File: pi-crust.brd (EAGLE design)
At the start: 41.9 x 40.4 mm, 10 parts

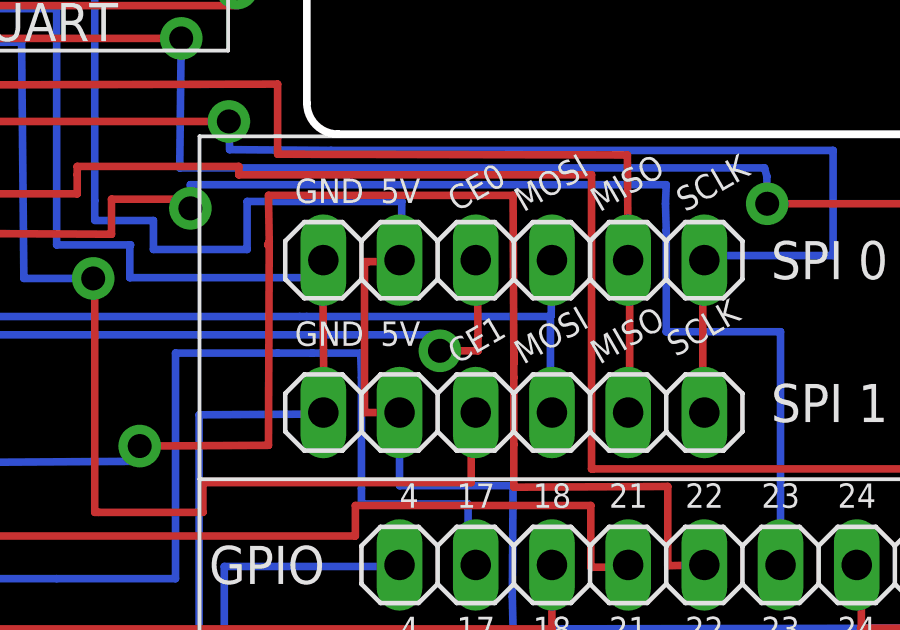
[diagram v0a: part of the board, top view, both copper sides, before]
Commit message: Moved one of the vias so its not so close to the headers.
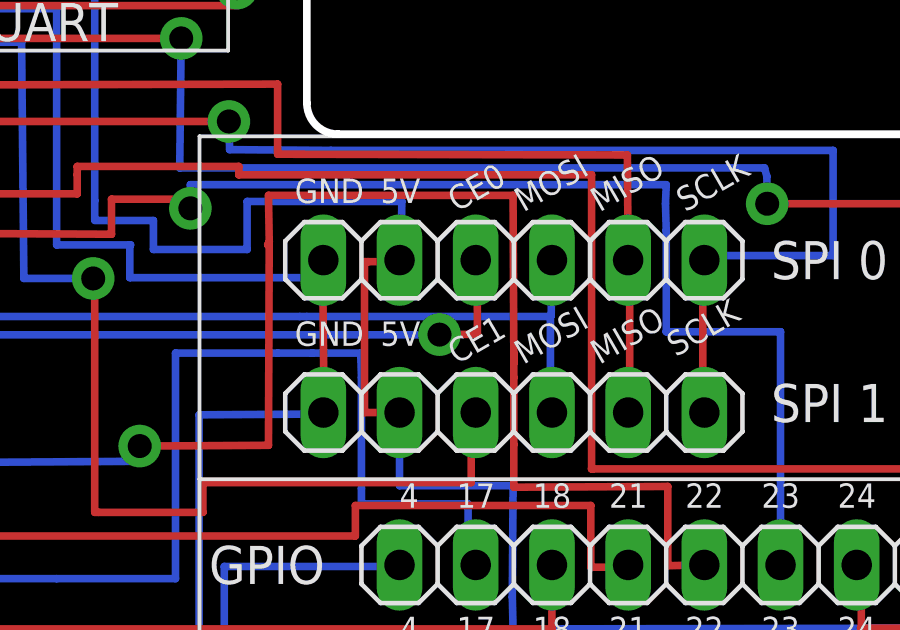
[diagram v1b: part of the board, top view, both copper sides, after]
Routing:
- net SPI_CE_0: track 34.8 -> 33.7 mm
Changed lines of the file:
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@@
 <setting verticaltext="up"/>
 </settings>
-<grid distance="0.02" unitdist="inch" unit="inch" style="lines" multiple="1" display="yes" altdistance="0.025" altunitdist="inch" altunit="inch"/>
+<grid distance="0" unitdist="inch" unit="inch" style="lines" multiple="1" display="yes" altdistance="0.025" altunitdist="inch" altunit="inch"/>
 <layers>
 <layer number="1" name="Top" color="4" fill="1" visible="yes" active="yes"/>
@@
 <wire x1="3.81" y1="23.7744" x2="7.8232" y2="23.7744" width="0.254" layer="16"/>
 <wire x1="24.1808" y1="26.6192" x2="23.9776" y2="26.6192" width="0.254" layer="1"/>
-<wire x1="24.2062" y1="24.13" x2="24.1808" y2="26.6192" width="0.254" layer="1"/>
-<wire x1="22.9362" y1="23.6474" x2="24.2062" y2="23.6474" width="0.254" layer="1"/>
-<wire x1="24.2062" y1="23.6474" x2="24.2062" y2="24.13" width="0.254" layer="1"/>
-<wire x1="22.7584" y1="23.6474" x2="22.9362" y2="23.6474" width="0.254" layer="16"/>
-<wire x1="22.7838" y1="24.1808" x2="22.7584" y2="23.6474" width="0.254" layer="16"/>
+<wire x1="24.18458125" y1="24.1948625" x2="24.1808" y2="26.6192" width="0.254" layer="1"/>
+<wire x1="22.9217875" y1="24.187909375" x2="22.901875" y2="24.195115625" width="0.254" layer="1"/>
+<wire x1="22.901875" y1="24.195115625" x2="24.18458125" y2="24.1948625" width="0.254" layer="1"/>
+<wire x1="22.880903125" y1="24.1807" x2="22.9217875" y2="24.187909375" width="0.254" layer="16"/>
+<wire x1="22.7838" y1="24.1808" x2="22.880903125" y2="24.1807" width="0.254" layer="16"/>
 <wire x1="7.8232" y1="24.1808" x2="22.7838" y2="24.1808" width="0.254" layer="16"/>
 <wire x1="7.8232" y1="23.7744" x2="7.8232" y2="24.1808" width="0.254" layer="16"/>
-<via x="22.9362" y="23.6474" extent="1-16" drill="0.8" diameter="1.4224"/>
+<via x="22.9217875" y="24.187909375" extent="1-16" drill="0.8" diameter="1.4224"/>
 </signal>
 <signal name="3V3">

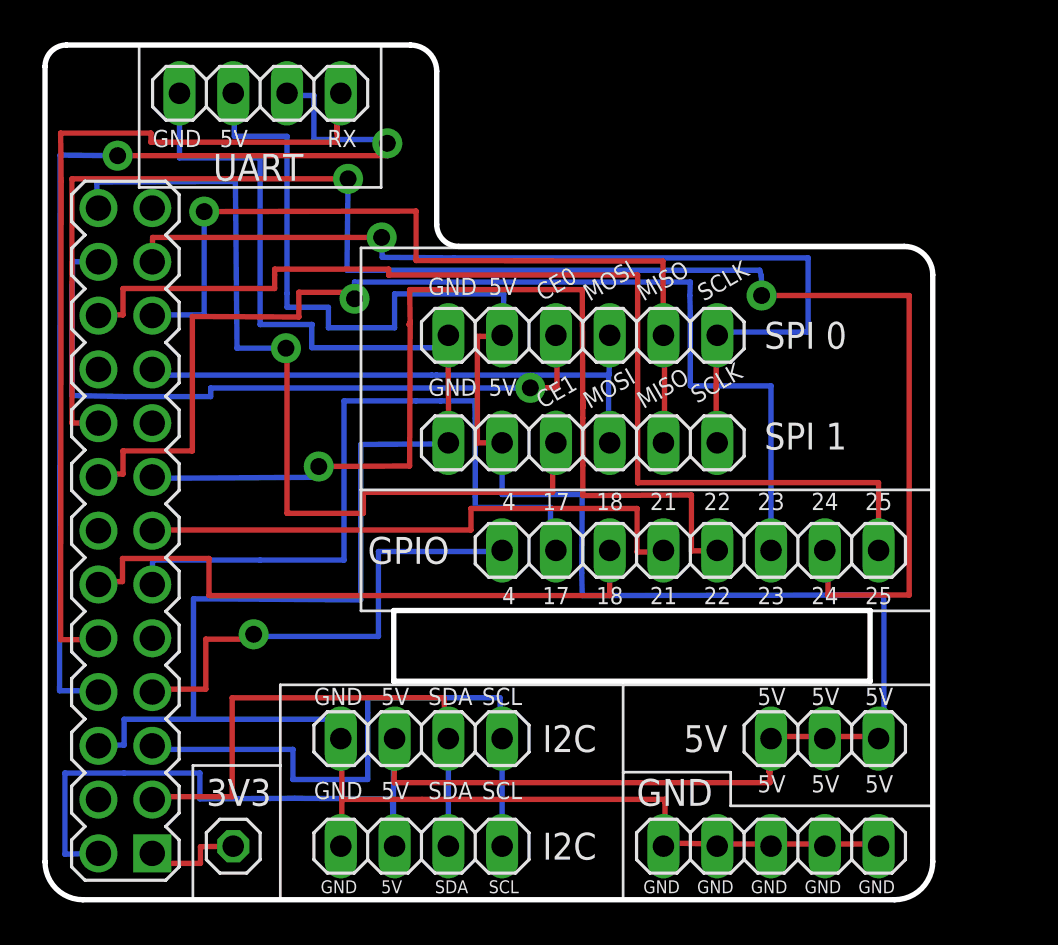
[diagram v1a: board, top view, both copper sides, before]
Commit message: Elongate board slot, as it was a wee bit too short.
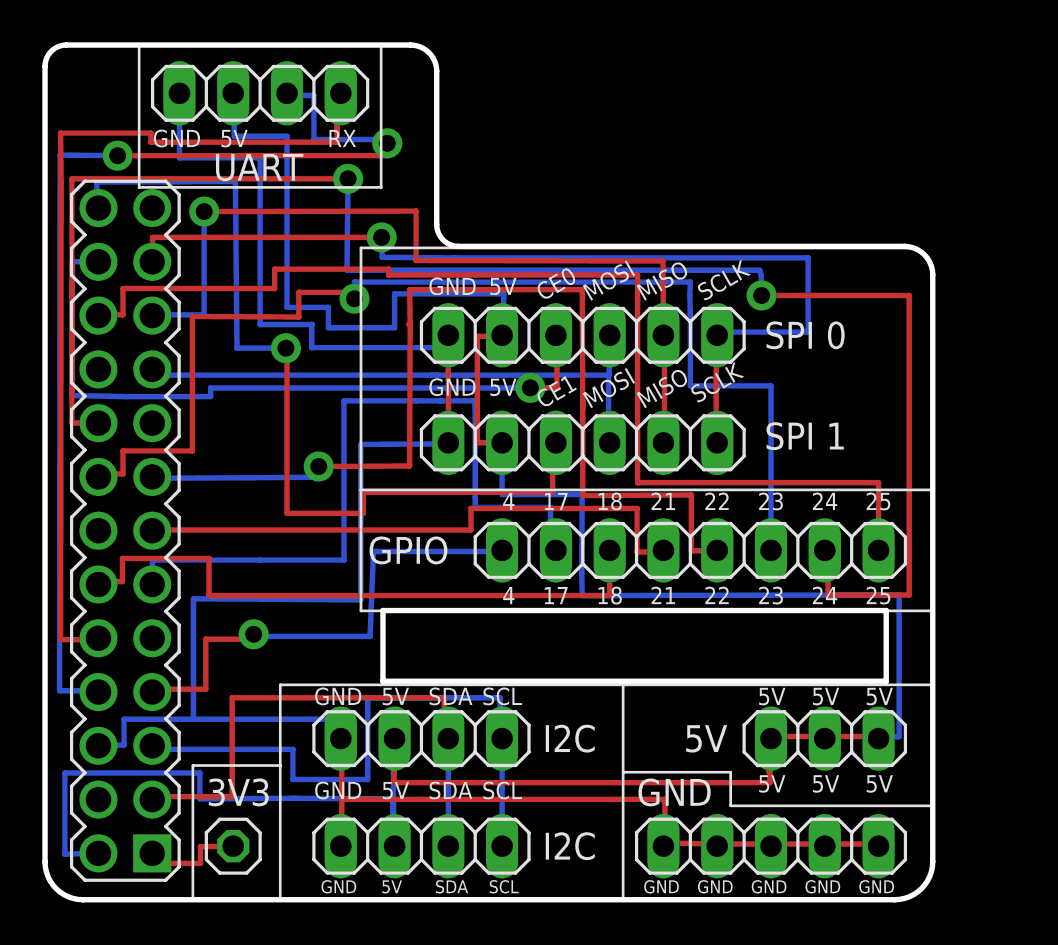
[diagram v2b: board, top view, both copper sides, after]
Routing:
- net 5V: track 123.9 -> 125.5 mm
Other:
- outline, holes or cut-outs redrawn
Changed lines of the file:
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@@
 <wire x1="1.7889" y1="0.01" x2="0" y2="1.7989" width="0.254" layer="20" curve="-90"/>
 <wire x1="0" y1="1.7989" x2="0" y2="39.37" width="0.254" layer="20"/>
-<wire x1="16.47" y1="10.34" x2="16.47" y2="13.68" width="0" layer="20"/>
-<wire x1="16.47" y1="10.33" x2="38.97" y2="10.33" width="0.254" layer="20"/>
-<wire x1="38.97" y1="10.33" x2="38.97" y2="13.67" width="0.254" layer="20"/>
-<wire x1="38.97" y1="13.67" x2="16.47" y2="13.67" width="0.254" layer="20"/>
-<wire x1="16.47" y1="13.67" x2="16.47" y2="10.33" width="0.254" layer="20"/>
+<wire x1="15.962" y1="10.34" x2="15.962" y2="13.68" width="0" layer="20"/>
+<wire x1="15.962" y1="10.33" x2="39.732" y2="10.33" width="0.254" layer="20"/>
+<wire x1="39.732" y1="10.33" x2="39.732" y2="13.67" width="0.254" layer="20"/>
+<wire x1="39.732" y1="13.67" x2="15.962" y2="13.67" width="0.254" layer="20"/>
+<wire x1="15.962" y1="13.67" x2="15.962" y2="10.34" width="0.254" layer="20"/>
+<wire x1="15.962" y1="10.34" x2="15.962" y2="10.33" width="0.254" layer="20"/>
 <wire x1="4.445" y1="40.3225" x2="4.445" y2="33.655" width="0.127" layer="25"/>
 <wire x1="4.445" y1="33.655" x2="15.875" y2="33.655" width="0.127" layer="25"/>
@@
 <contactref element="JP5" pad="1"/>
 <contactref element="JP1" pad="7"/>
-<wire x1="15.748" y1="16.4592" x2="21.5392" y2="16.4592" width="0.254" layer="16"/>
+<wire x1="15.5147375" y1="16.4592" x2="21.5392" y2="16.4592" width="0.254" layer="16"/>
 <wire x1="5.0643" y1="9.8198" x2="5.08" y2="9.9568" width="0.254" layer="1"/>
 <wire x1="21.5392" y1="16.4592" x2="21.59" y2="16.51" width="0.254" layer="16"/>
-<wire x1="15.748" y1="12.446" x2="15.748" y2="16.4592" width="0.254" layer="16"/>
+<wire x1="15.353246875" y1="12.446" x2="15.5147375" y2="16.4592" width="0.254" layer="16"/>
 <wire x1="5.08" y1="9.9568" x2="7.5946" y2="9.9568" width="0.254" layer="1"/>
 <wire x1="7.5946" y1="9.9568" x2="7.5946" y2="12.319" width="0.254" layer="1"/>
 <wire x1="7.5946" y1="12.319" x2="9.8552" y2="12.319" width="0.254" layer="1"/>
 <wire x1="9.8552" y1="12.319" x2="9.8552" y2="12.5476" width="0.254" layer="1"/>
-<wire x1="9.8552" y1="12.446" x2="15.748" y2="12.446" width="0.254" layer="16"/>
+<wire x1="9.8552" y1="12.446" x2="15.353246875" y2="12.446" width="0.254" layer="16"/>
 <wire x1="9.8552" y1="12.5476" x2="9.8552" y2="12.446" width="0.254" layer="16"/>
 <via x="9.8552" y="12.5476" extent="1-16" drill="0.8" diameter="1.4224"/>
@@
 <contactref element="JP3" pad="3"/>
 <contactref element="JP1" pad="2"/>
-<wire x1="8.9408" y1="36.3728" x2="8.9408" y2="37.9984" width="0.254" layer="16"/>
+<wire x1="8.9408" y1="36.068" x2="8.9408" y2="37.9984" width="0.254" layer="16"/>
 <wire x1="21.6408" y1="26.67" x2="21.6662" y2="28.6258" width="0.254" layer="16"/>
 <wire x1="8.9408" y1="37.9984" x2="8.89" y2="38.1" width="0.254" layer="16"/>
@@
 <wire x1="16.4084" y1="4.7752" x2="16.4592" y2="2.6416" width="0.254" layer="16"/>
 <wire x1="2.5243" y1="2.1998" x2="2.4892" y2="2.2098" width="0.254" layer="16"/>
-<wire x1="16.4592" y1="2.6416" x2="16.4592" y2="5.5626" width="0.254" layer="16"/>
-<wire x1="16.4592" y1="5.5626" x2="16.4592" y2="7.5184" width="0.254" layer="16"/>
+<wire x1="16.4592" y1="2.6416" x2="16.4592" y2="7.5184" width="0.254" layer="16"/>
 <wire x1="16.4592" y1="7.5184" x2="16.51" y2="7.62" width="0.254" layer="16"/>
 <wire x1="16.4592" y1="2.6416" x2="16.51" y2="2.54" width="0.254" layer="16"/>
@@
 <wire x1="25.3746" y1="14.3764" x2="25.3492" y2="15.4432" width="0.254" layer="16"/>
 <wire x1="39.5986" y1="14.4018" x2="25.3746" y2="14.3764" width="0.254" layer="16"/>
-<wire x1="39.624" y1="14.0208" x2="39.5986" y2="14.4018" width="0.254" layer="16"/>
-<wire x1="39.624" y1="7.9248" x2="39.624" y2="14.0208" width="0.254" layer="16"/>
-<wire x1="39.4208" y1="7.7216" x2="39.624" y2="7.9248" width="0.254" layer="16"/>
+<wire x1="40.341775" y1="14.409978125" x2="39.5986" y2="14.4018" width="0.254" layer="16"/>
+<wire x1="40.34165625" y1="7.709496875" x2="40.341775" y2="14.409978125" width="0.254" layer="16"/>
+<wire x1="39.4208" y1="7.7216" x2="40.34165625" y2="7.709496875" width="0.254" layer="16"/>
 <wire x1="21.59" y1="21.59" x2="21.7424" y2="21.5392" width="0.254" layer="16"/>
 <wire x1="39.37" y1="7.62" x2="39.4208" y2="7.7216" width="0.254" layer="16"/>
 <wire x1="25.3746" y1="19.1516" x2="21.59" y2="19.1516" width="0.254" layer="16"/>
 <wire x1="21.59" y1="19.1516" x2="21.59" y2="21.59" width="0.254" layer="16"/>
-<wire x1="11.43" y1="28.6512" x2="11.43" y2="36.068" width="0.254" layer="16"/>
+<wire x1="11.43" y1="28.0162" x2="11.43" y2="36.068" width="0.254" layer="16"/>
 <wire x1="11.43" y1="36.068" x2="8.9408" y2="36.068" width="0.254" layer="16"/>
-<wire x1="8.9408" y1="36.068" x2="8.9408" y2="36.3728" width="0.254" layer="16"/>
 <wire x1="21.59" y1="21.59" x2="20.4216" y2="21.59" width="0.254" layer="1"/>
-<wire x1="20.5486" y1="26.6192" x2="21.59" y2="26.6192" width="0.254" layer="1"/>
+<wire x1="20.4216" y1="26.6192" x2="21.59" y2="26.6192" width="0.254" layer="1"/>
 <wire x1="21.59" y1="26.6192" x2="21.59" y2="26.67" width="0.254" layer="1"/>
-<wire x1="11.43" y1="28.0162" x2="11.43" y2="28.6512" width="0.254" layer="16"/>
-<wire x1="20.4216" y1="26.6192" x2="20.5486" y2="26.6192" width="0.254" layer="1"/>
 <wire x1="20.4216" y1="21.59" x2="20.4216" y2="26.6192" width="0.254" layer="1"/>
 <wire x1="21.6662" y1="28.6258" x2="16.51" y2="28.6258" width="0.254" layer="16"/>
@@
 <wire x1="2.4892" y1="2.2098" x2="0.9398" y2="2.159" width="0.254" layer="16"/>
 <wire x1="0.9398" y1="2.159" x2="0.9398" y2="5.9944" width="0.254" layer="16"/>
-<wire x1="0.9398" y1="5.9944" x2="3.7338" y2="5.9944" width="0.254" layer="16"/>
-<wire x1="3.7338" y1="5.9944" x2="7.3152" y2="5.9944" width="0.254" layer="16"/>
+<wire x1="0.9398" y1="5.9944" x2="7.3152" y2="5.9944" width="0.254" layer="16"/>
 <wire x1="7.3152" y1="5.9944" x2="7.3152" y2="4.7752" width="0.254" layer="16"/>
 <wire x1="11.43" y1="27.9908" x2="11.43" y2="28.0162" width="0" layer="19" extent="16-16"/>

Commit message: PiCrust V2:
* Made 26 pin connector pads square, so it's easy to dab solder over
  the edges of the pin inserts.
* Vias are smaller and tented.
* Minor re-routing around some tight areas.
* Added text to silk screen.
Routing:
- net 5V: track 125.5 -> 127.2 mm
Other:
- board text added: "PiCrust v2"
- board text added: "Think inside the box"
- board text added: "waln.es/picrust"

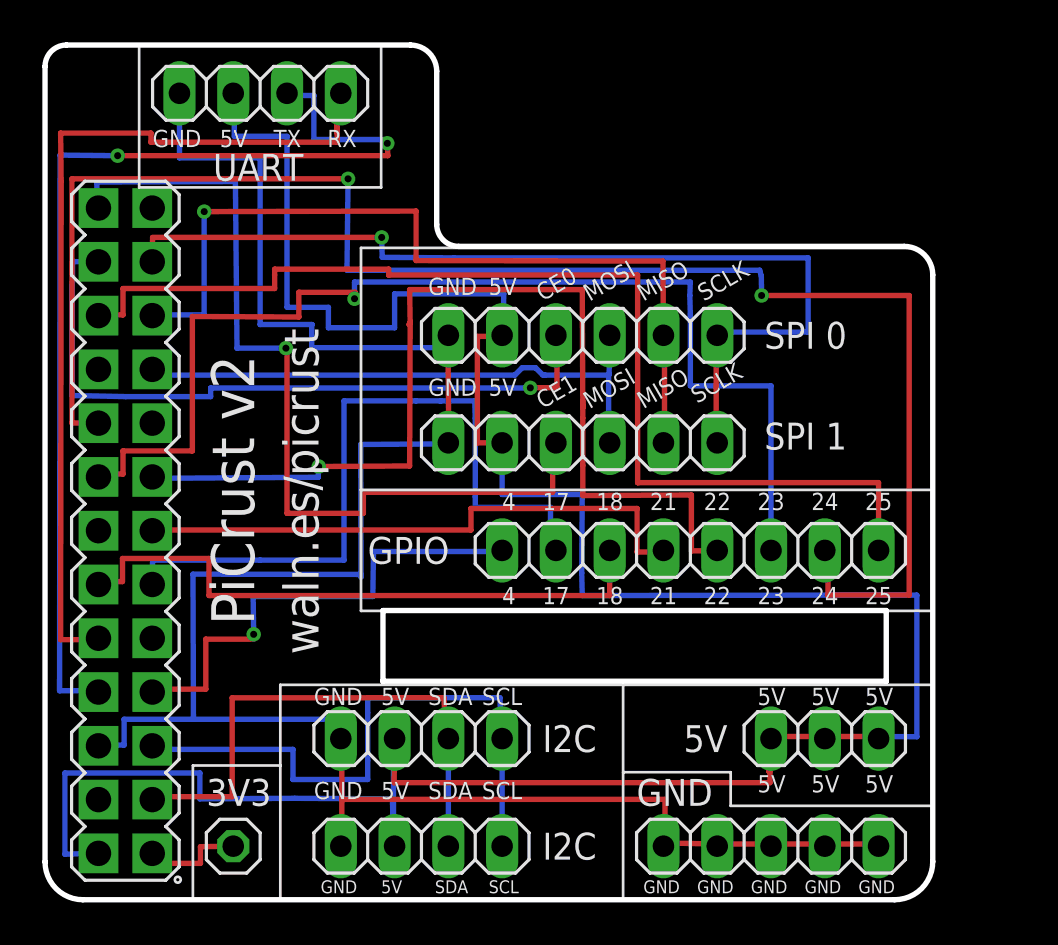
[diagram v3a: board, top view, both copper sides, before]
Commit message: v3 board. With Hirose 26 pin connector.
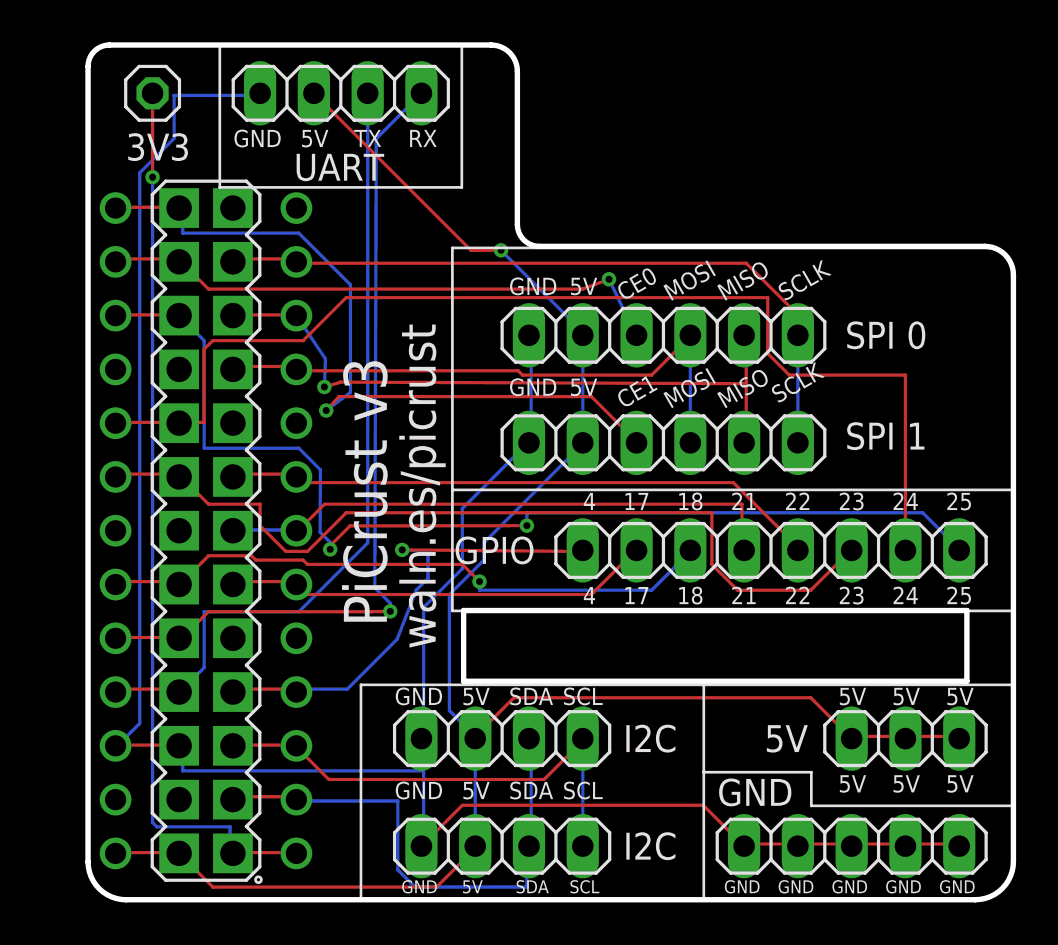
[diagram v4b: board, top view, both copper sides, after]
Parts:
- added U$1: MDF7-26D-2.54DSA, E-test-solutions (5):MDF7-26D-2.54DSA
- moved JP4 35.8 mm to (5.08, 38.1)
- moved JP2 3.81 mm to (38.1, 2.54)
- moved JP3 3.81 mm to (40.6, 7.62)
- moved JP7 3.81 mm to (29.2, 26.7)
- moved JP8 3.81 mm to (29.2, 21.6)
- moved JP1 3.81 mm to (7.60, 17.4)
- moved JP6 3.81 mm to (14.0, 38.1)
- moved JP10 3.81 mm to (21.6, 2.54)
- moved JP5 3.81 mm to (34.3, 16.5)
- moved JP9 3.81 mm to (21.6, 7.62)
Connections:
- net 3V3: now also U$1.P$1
- net 5V: now also U$1.P$14
- net GND: now also U$1.P$16
- net GPIO_04: now also U$1.P$4
- net GPIO_17: now also U$1.P$6
- net GPIO_18: now also U$1.P$19
- net GPIO_21: now also U$1.P$7
- net GPIO_22: now also U$1.P$8
- net GPIO_23: now also U$1.P$21
- net GPIO_24: now also U$1.P$22
- net GPIO_25: now also U$1.P$24
- net I2C_SCL: now also U$1.P$3
- net I2C_SDA: now also U$1.P$2
- net SPI_CE_0: now also U$1.P$25
- net SPI_CE_1: now also U$1.P$26
- net SPI_MISO: now also U$1.P$11
- net SPI_MOSI: now also U$1.P$10
- net SPI_SCLK: now also U$1.P$12
- net UART_RX: now also U$1.P$18
- net UART_TX: now also U$1.P$17
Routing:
- net 5V: track 127.2 -> 88.0 mm, vias 0 -> 1
- net 3V3: track 5.12 -> 42.6 mm, vias 0 -> 1
- net GPIO_24: track 78.1 -> 53.1 mm, vias 2 -> 0
- net GPIO_22: track 48.5 -> 28.4 mm, vias 1 -> 0
- net GPIO_17: track 34.8 -> 20.3 mm
- net GPIO_23: track 54.2 -> 41.4 mm, vias 1 -> 0
- net UART_TX: track 50.5 -> 37.8 mm, vias 2 -> 0
- net SPI_SCLK: track 46.1 -> 33.9 mm, vias 1 -> 0
- net SPI_MISO: track 40.0 -> 31.9 mm
- net SPI_CE_0: track 33.7 -> 27.0 mm
- net SPI_CE_1: track 42.1 -> 35.6 mm
- net I2C_SCL: track 28.9 -> 23.2 mm
- net UART_RX: track 42.1 -> 39.2 mm, vias 0 -> 1
- net GND: track 103.4 -> 105.5 mm
- net GPIO_25: track 52.3 -> 51.3 mm, vias 0 -> 2
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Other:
- board size 41.9 x 40.4 mm -> 43.7 x 40.4 mm
- board text added: "PiCrust v3"
- board text removed: "PiCrust v2"
